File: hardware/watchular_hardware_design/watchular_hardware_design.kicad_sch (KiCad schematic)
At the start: 27 parts, among them J1 USB4105-GF-A, U1 ESP32-C3FH4, U2 MIC5524-3.3YMT-TZ, U3 W25Q16JVSSIQ, Y1 40MHz

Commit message: Added 15 position 2.45mm headers.
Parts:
- added J2, J3: TSW-115-07-H-S, SAMTEC_TSW-115-07-H-S, symbol TSW-115-07-H-S:TSW-115-07-H-S
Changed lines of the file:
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@@
     (pin "1")
+  )
+  (symbol (lib_id "TSW-115-07-H-S:TSW-115-07-H-S") (at 163.83 135.89 0) (unit 1)
+    (in_bom yes) (on_board yes) (fields_autoplaced)
+    (property "Reference" "J3" (id 0) (at 173.355 134.6199 0)
+      (effects (font (size 1.27 1.27)) (justify left))
+    )
+    (property "Value" "TSW-115-07-H-S" (id 1) (at 173.355 137.1599 0)
+      (effects (font (size 1.27 1.27)) (justify left))
+    )
+    (property "Footprint" "SAMTEC_TSW-115-07-H-S" (id 2) (at 163.83 135.89 0)
+      (effects (font (size 1.27 1.27)) (justify left bottom) hide)
+    )
+    (property "Datasheet" "" (id 3) (at 163.83 135.89 0)
+      (effects (font (size 1.27 1.27)) (justify left bottom) hide)
+    )
+    (property "PARTREV" "R" (id 4) (at 163.83 135.89 0)
+      (effects (font (size 1.27 1.27)) (justify left bottom) hide)
+    )
+    (property "MANUFACTURER" "Samtec" (id 5) (at 163.83 135.89 0)
+      (effects (font (size 1.27 1.27)) (justify left bottom) hide)
+    )
+    (property "STANDARD" "Manufacturer Recommendations" (id 6) (at 163.83 135.89 0)
+      (effects (font (size 1.27 1.27)) (justify left bottom) hide)
+    )
+    (pin "01")
+    (pin "02")
+    (pin "03")
+    (pin "04")
+    (pin "05")
+    (pin "06")
+    (pin "07")
+    (pin "08")
+    (pin "09")
+    (pin "10")
+    (pin "11")
+    (pin "12")
+    (pin "13")
+    (pin "14")
+    (pin "15")
   )
   (symbol (lib_id "power:+3.3V") (at 114.3 67.31 0) (unit 1)
@@
     )
     (pin "1")
+  )
+  (symbol (lib_id "TSW-115-07-H-S:TSW-115-07-H-S") (at 163.195 88.9 0) (unit 1)
+    (in_bom yes) (on_board yes) (fields_autoplaced)
+    (property "Reference" "J2" (id 0) (at 172.72 87.6299 0)
+      (effects (font (size 1.27 1.27)) (justify left))
+    )
+    (property "Value" "TSW-115-07-H-S" (id 1) (at 172.72 90.1699 0)
+      (effects (font (size 1.27 1.27)) (justify left))
+    )
+    (property "Footprint" "SAMTEC_TSW-115-07-H-S" (id 2) (at 163.195 88.9 0)
+      (effects (font (size 1.27 1.27)) (justify left bottom) hide)
+    )
+    (property "Datasheet" "" (id 3) (at 163.195 88.9 0)
+      (effects (font (size 1.27 1.27)) (justify left bottom) hide)
+    )
+    (property "PARTREV" "R" (id 4) (at 163.195 88.9 0)
+      (effects (font (size 1.27 1.27)) (justify left bottom) hide)
+    )
+    (property "MANUFACTURER" "Samtec" (id 5) (at 163.195 88.9 0)
+      (effects (font (size 1.27 1.27)) (justify left bottom) hide)
+    )
+    (property "STANDARD" "Manufacturer Recommendations" (id 6) (at 163.195 88.9 0)
+      (effects (font (size 1.27 1.27)) (justify left bottom) hide)
+    )
+    (pin "01")
+    (pin "02")
+    (pin "03")
+    (pin "04")
+    (pin "05")
+    (pin "06")
+    (pin "07")
+    (pin "08")
+    (pin "09")
+    (pin "10")
+    (pin "11")
+    (pin "12")
+    (pin "13")
+    (pin "14")
+    (pin "15")
   )
   (symbol (lib_id "power:+5V") (at 152.908 26.67 0) (unit 1)
@@
       (reference "#PWR028") (unit 1) (value "+3.3VA") (footprint "")
     )
+    (path "/4564b4f9-90bf-45c2-8acf-66350b5ba946/21322b11-972f-4c4d-8d2c-95827ad64aa3"
+      (reference "#PWR029") (unit 1) (value "GND") (footprint "")
+    )
+    (path "/4564b4f9-90bf-45c2-8acf-66350b5ba946/5ae09de8-32ce-4d21-91aa-6ca5ffb4b2b8"
+      (reference "#PWR030") (unit 1) (value "GND") (footprint "")
+    )
     (path "/4564b4f9-90bf-45c2-8acf-66350b5ba946/39176a5a-bace-4dce-bfe2-de9ed80c862d"
-      (reference "#PWR029") (unit 1) (value "GND") (footprint "")
+      (reference "#PWR031") (unit 1) (value "GND") (footprint "")
     )
     (path "/4564b4f9-90bf-45c2-8acf-66350b5ba946/3f4e7940-f12b-43b6-a231-2830bdb19a41"
-      (reference "#PWR030") (unit 1) (value "GND") (footprint "")
+      (reference "#PWR032") (unit 1) (value "GND") (footprint "")
     )
     (path "/4564b4f9-90bf-45c2-8acf-66350b5ba946/97dd204e-2a06-4a2b-a41c-0bb1913eca42"
-      (reference "#PWR031") (unit 1) (value "GND") (footprint "")
+      (reference "#PWR033") (unit 1) (value "GND") (footprint "")
     )
     (path "/4564b4f9-90bf-45c2-8acf-66350b5ba946/f766da9c-a2d4-4ea2-91de-56ef56d471fe"
-      (reference "#PWR032") (unit 1) (value "GND") (footprint "")
-    )
-    (path "/4564b4f9-90bf-45c2-8acf-66350b5ba946/21322b11-972f-4c4d-8d2c-95827ad64aa3"
-      (reference "#PWR0101") (unit 1) (value "GND") (footprint "")
-    )
-    (path "/4564b4f9-90bf-45c2-8acf-66350b5ba946/5ae09de8-32ce-4d21-91aa-6ca5ffb4b2b8"
-      (reference "#PWR0102") (unit 1) (value "GND") (footprint "")
+      (reference "#PWR034") (unit 1) (value "GND") (footprint "")
     )
     (path "/1139fd41-bcfc-4cbe-8f9a-b980537f1914"
@@
       (reference "J1") (unit 1) (value "USB4105-GF-A") (footprint "USBC-USB4105-GF-A:GCT_USB4105-GF-A")
     )
-    (path "/4564b4f9-90bf-45c2-8acf-66350b5ba946/bcf8fc21-2e6f-4838-871d-7ce6d0592d88"
-      (reference "J?") (unit 1) (value "TSW-116-07-H-S") (footprint "SAMTEC_TSW-116-07-H-S")
+    (path "/aaba2395-6f74-4d9b-a7b1-0de3734b29d9"
+      (reference "J2") (unit 1) (value "TSW-115-07-H-S") (footprint "SAMTEC_TSW-115-07-H-S")
+    )
+    (path "/2fe71312-324c-4c14-a7b3-7e98b4bcfd9d"
+      (reference "J3") (unit 1) (value "TSW-115-07-H-S") (footprint "SAMTEC_TSW-115-07-H-S")
     )
     (path "/1f1de665-878b-408f-bbe7-a6c746e0bfb6"

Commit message: Connected MCU pins to the brekout 15 pos header.
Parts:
- removed J2, J3: TSW-115-07-H-S, SAMTEC_TSW-115-07-H-S, symbol TSW-115-07-H-S:TSW-115-07-H-S
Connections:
- net CHIP_EN: now reaches R3.2, U1.7 (CHIP_EN)

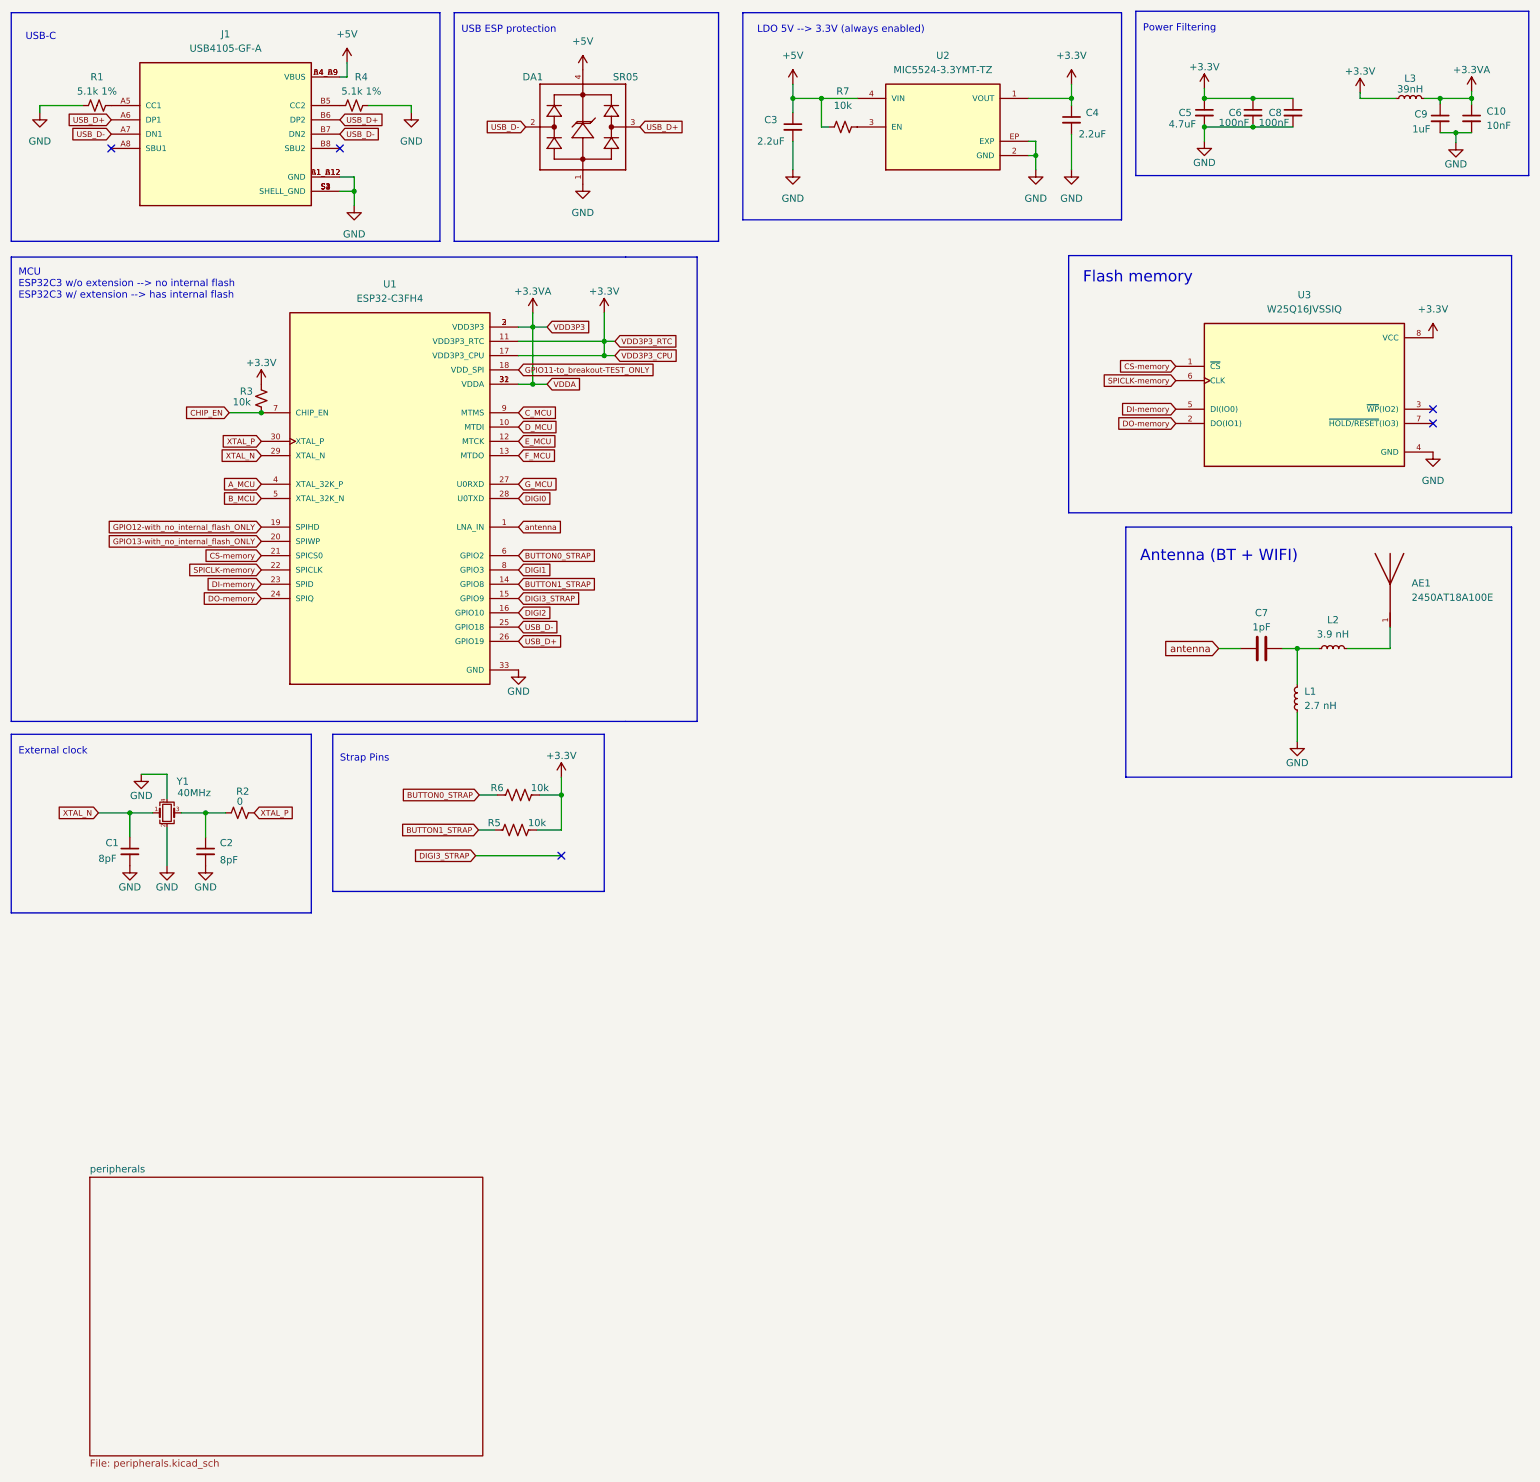
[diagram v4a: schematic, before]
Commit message: Added mosfet for controlling the power source.
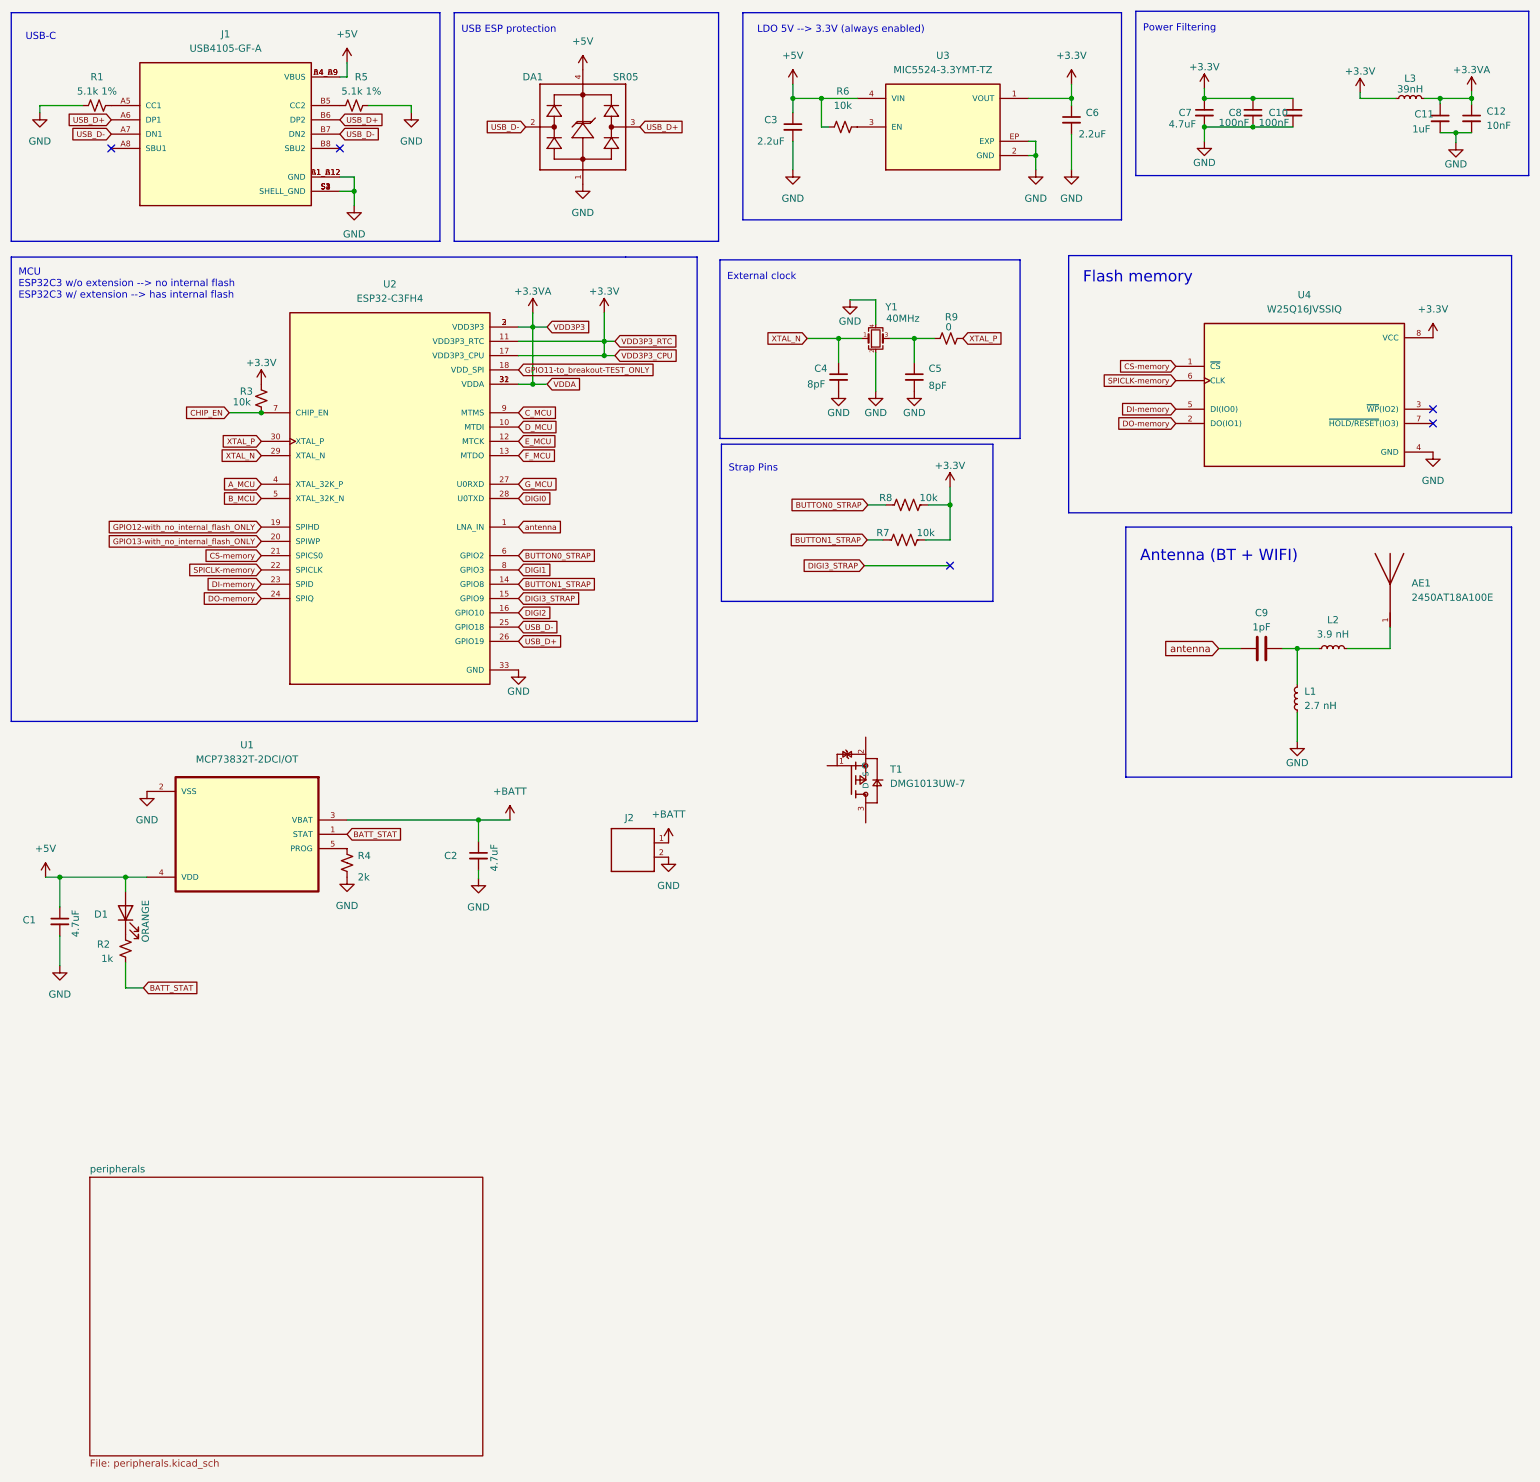
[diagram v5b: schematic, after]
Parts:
- added C1, C2: 4.7uF, Capacitor_SMD:C_0402_1005Metric_Pad0.74x0.62mm_HandSolder, symbol Device:C_Small
- added D1: ORANGE, LED_SMD:LED_0402_1005Metric_Pad0.77x0.64mm_HandSolder, symbol Device:LED
- added J2: 665102131822, battery_connector-665102131822:665102131822, symbol 665102131822:665102131822
- added R2: 1k, Resistor_SMD:R_0402_1005Metric_Pad0.72x0.64mm_HandSolder, symbol Device:R_Small_US
- added R4: 2k, Resistor_SMD:R_0402_1005Metric_Pad0.72x0.64mm_HandSolder, symbol Device:R_Small_US
- added T1: DMG1013UW-7, SOT-323, symbol DMG1013UW-7:DMG1013UW-7
- added U1: MCP73832T-2DCI/OT, battery_charger-MCP73832T:SOT95P280X145-5N, symbol MCP73832T-2DCI_OT:MCP73832T-2DCI/OT
- renumbered C8 to C10, C9 to C11, C10 to C12, C1 to C4, C2 to C5, C4 to C6, C5 to C7, C6 to C8, C7 to C9, R4 to R5, R7 to R6, R5 to R7, R6 to R8, R2 to R9, U1 to U2, U2 to U3, U3 to U4
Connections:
- net +5V: now also C1.1, D1.2 (A), U1.4 (VDD)
- net GND: now also C1.2, C2.2, J2.2, R4.2, U1.2 (VSS)
- new net: D1.1 (K), R2.1
- new net: R4.1, U1.5 (PROG)
- new net +BATT: C2.1, J2.1, U1.3 (VBAT)
- new net BATT_STAT: R2.2, U1.1 (STAT)
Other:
- moved on the sheet: C4, C5, R7, R8, R9, Y1

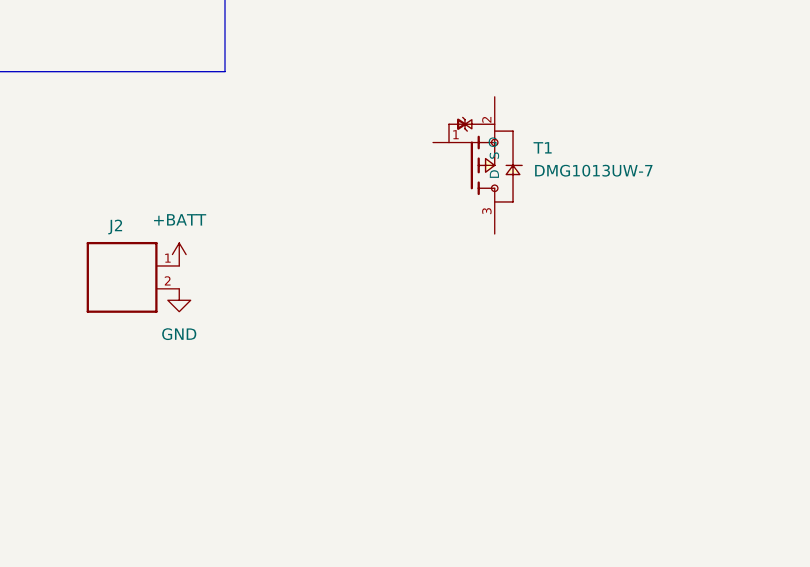
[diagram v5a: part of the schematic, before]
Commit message: Added schottky diode.
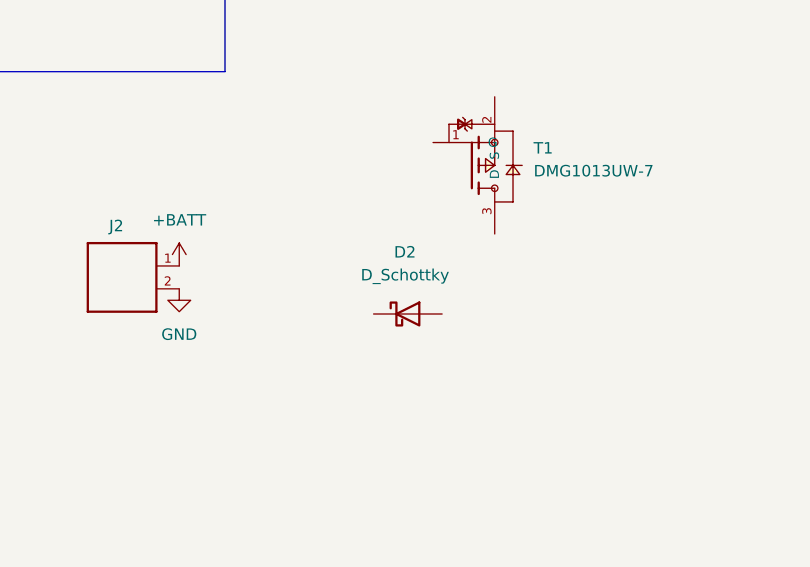
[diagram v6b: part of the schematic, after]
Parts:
- added D2: D_Schottky, Diode_SMD:D_SOD-123F, symbol Device:D_Schottky
- AE1: footprint ANTC3216X140N -> ANT-2450AT18A100E:ANTC3216X140N
- T1: footprint SOT-323 -> P_MOSFET-DMG1013UW:SOT-323
- U2: footprint QFN50P500X500X90-33N -> ESP32-C3:QFN50P500X500X90-33N
